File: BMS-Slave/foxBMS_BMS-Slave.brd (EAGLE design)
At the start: 120 x 110 mm, 391 parts, among them IC1401 CPC1008N, IC1402 CPC1008N, IC1403 CPC1008N, IC1404 CPC1008N, IC1405 CPC1008N, IC1406 CPC1008N, IC1407 CPC1008N, IC1408 CPC1008N, IC1409 CPC1008N, IC1410 CPC1008N, IC1411 CPC1008N, IC1412 CPC1008N, IC1701 24AA02UID, IC1801 24AA02UID, IC201 LTC6804HG-1#PBF, IC301 LTC6804HG-1#PBF, M1001 LTC1380CGN, M1002 LTC1380CGN, M1101 LTC1380CGN, M1102 LTC1380CGN, M1301 LTC1380CGN, M1302 LTC1380CGN, M1401 LTC1380CGN, M1402 LTC1380CGN, T1201 NX2301P, T1202 NX2301P, T1203 NX2301P, T1204 NX2301P, T1205 NX2301P, T1206 NX2301P, T1207 NX2301P, T1208 NX2301P, T1209 NX2301P, T1210 NX2301P, T1211 NX2301P, T1212 NX2301P, T401 PBHV8115Z, T501 PBHV8115Z, X1601 43045-0406_MOLEX_4PIN, X1602 43045-0406_MOLEX_4PIN, X1603 43045-1606_MOLEX_16PIN, X1604 MA10-2, X1605 MA09-2, X1606 43045-2406_MOLEX_24PIN, X1607 MA10-2, X1608 MA10-2

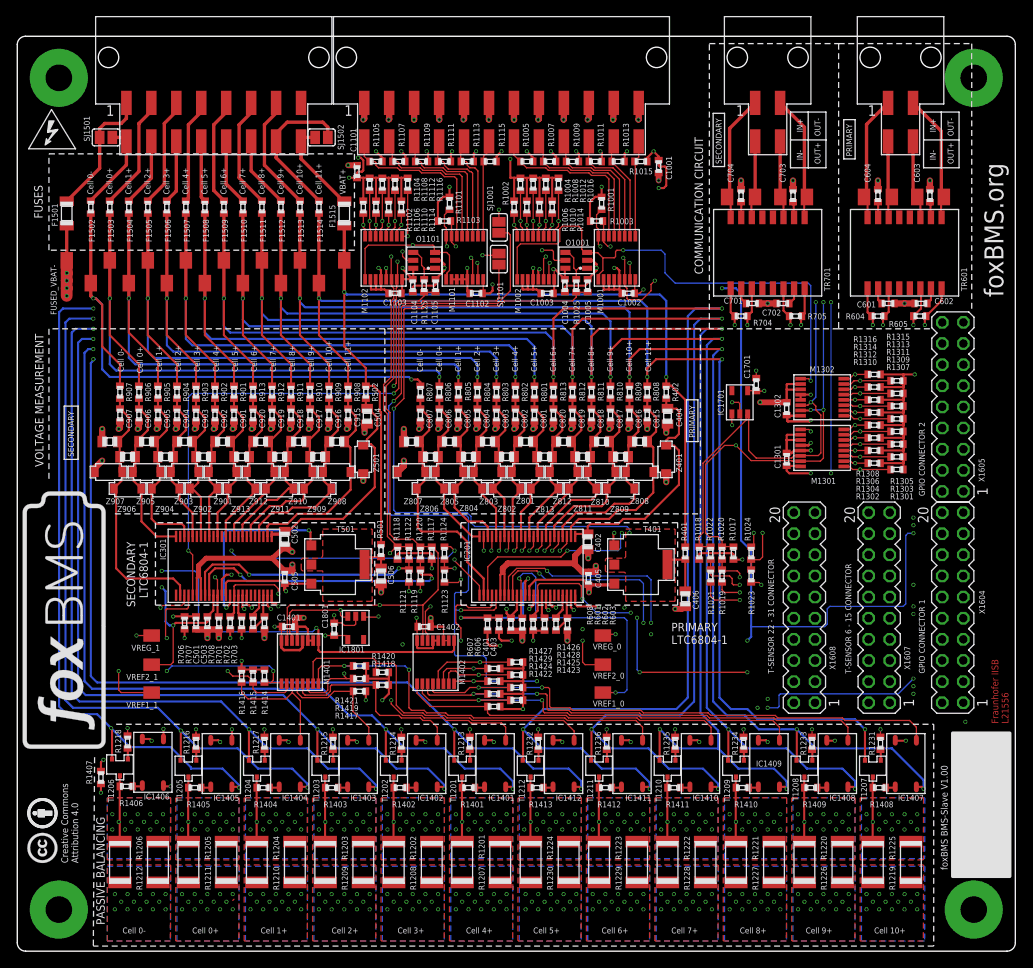
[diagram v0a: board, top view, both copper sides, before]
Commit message: Minor updates and corrections of notations, wording and bill of materials (V1.0.1). No changes in schematic and layout.
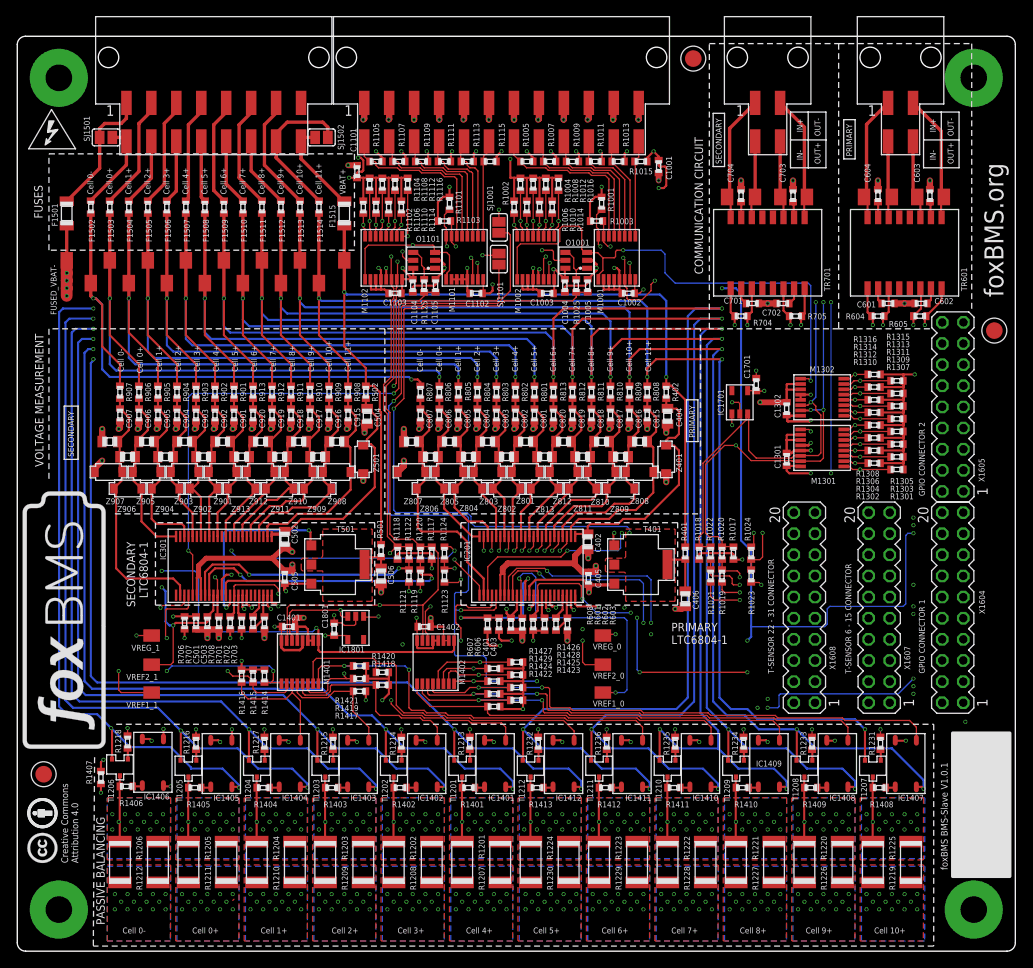
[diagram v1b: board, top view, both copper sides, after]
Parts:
- added U$50, U$52, U$62: (no value), foxBMS_BMS-Slave_12cell:FIDUCIAL_1MM
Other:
- board text added: "foxBMS BMS-Slave V1.0.1"
- board text removed: "Fraunhofer IISB L21556"
- board text removed: "foxBMS BMS-Slave V1.00"
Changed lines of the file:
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@@
 <layer number="27" name="tValues" color="7" fill="1" visible="no" active="yes"/>
 <layer number="28" name="bValues" color="7" fill="1" visible="no" active="yes"/>
-<layer number="29" name="tStop" color="7" fill="3" visible="no" active="yes"/>
+<layer number="29" name="tStop" color="7" fill="3" visible="yes" active="yes"/>
 <layer number="30" name="bStop" color="7" fill="6" visible="no" active="yes"/>
 <layer number="31" name="tCream" color="7" fill="4" visible="no" active="yes"/>
@@
 <layer number="250" name="Descript" color="3" fill="1" visible="yes" active="yes"/>
 <layer number="251" name="SMDround" color="7" fill="1" visible="no" active="yes"/>
+<layer number="253" name="Insertarea2" color="7" fill="1" visible="yes" active="yes"/>
 <layer number="254" name="OrgLBR" color="13" fill="1" visible="no" active="yes"/>
+<layer number="255" name="HELP" color="11" fill="1" visible="yes" active="yes"/>
 </layers>
 <board>
@@
 <vertex x="4.036903125" y="97.3836"/>
 </polygon>
-<text x="119.1768" y="27.3558" size="0.8128" layer="1" font="vector" rot="R90">Fraunhofer IISB
-L21556</text>
-<text x="119.1768" y="27.3558" size="0.8128" layer="29" font="vector" rot="R90">Fraunhofer IISB
-L21556</text>
 <polygon width="0.0254" layer="25">
 <vertex x="3.394309375" y="54.27186875"/>
@@
 <vertex x="112.4712" y="8.9916"/>
 </polygon>
-<text x="111.8616" y="9.7536" size="0.8128" layer="25" rot="R90">foxBMS BMS-Slave V1.00</text>
+<text x="111.8616" y="9.7536" size="0.8128" layer="25" rot="R90">foxBMS BMS-Slave V1.0.1</text>
 <text x="118.5672" y="78.6384" size="2.286" layer="25" rot="R90">foxBMS.org</text>
 <polygon width="0.0254" layer="25">
@@
 <attribute name="NAME" x="17.526" y="48.3108" size="0.7112" layer="25" font="vector" ratio="10" rot="R270" align="center"/>
 </element>
+<element name="U$50" library="foxBMS_BMS-Slave_12cell" package="FIDUCIAL_1MM" value="" x="3.175" y="21.2725"/>
+<element name="U$52" library="foxBMS_BMS-Slave_12cell" package="FIDUCIAL_1MM" value="" x="117.475" y="74.6125"/>
+<element name="U$62" library="foxBMS_BMS-Slave_12cell" package="FIDUCIAL_1MM" value="" x="81.28" y="107.315"/>
 </elements>
 <signals>
